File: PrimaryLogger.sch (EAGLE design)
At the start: 48 parts, among them J1 CONN_42.54_SCREW, J2 CONN_42.54_SCREW, J3 CONN_42.54_SCREW, J4 CONN_42.54_SCREW, J5 CONN_32.54_SCREW, U1 MIC2005, U2 MIC2091, U25 SN74AUP3G34DCU, U3 TPL5010DDC, U4 TXS0102DCU, U5 SN74LVC1G3157DRL, U6 TCS3400, U7 SHTC3DFN

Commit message: Continued layout progress
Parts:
- C1, C2: value (none) -> 6pF
- XTAL1: DIGIKEY (none) -> 535-11937-1-ND; MF (none) -> ABS07-120-32.768KHZ-T; MPN (none) -> Abracon
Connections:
- new net GPIOXA: J5.2, MS1.GPIOA3
- new net N$10: MS1.GPIOA5
- new net N$9: MS1.GPIOA4
- net 3V3_EXT: now also J5.1
- net GND: now also J5.3
- net GPIO1A: now also MS1.GPIOA0
- net GPIO2A: now also MS1.GPIOA1
- net GPIO3A: now also MS1.GPIOA2
- net MISO: now also MS1.GPIOMISO
- net MOSI: now also MS1.GPIOMOSI
- net SCK: now also MS1.GPIOSCK
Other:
- moved on the sheet: J6, J7, J8, R8

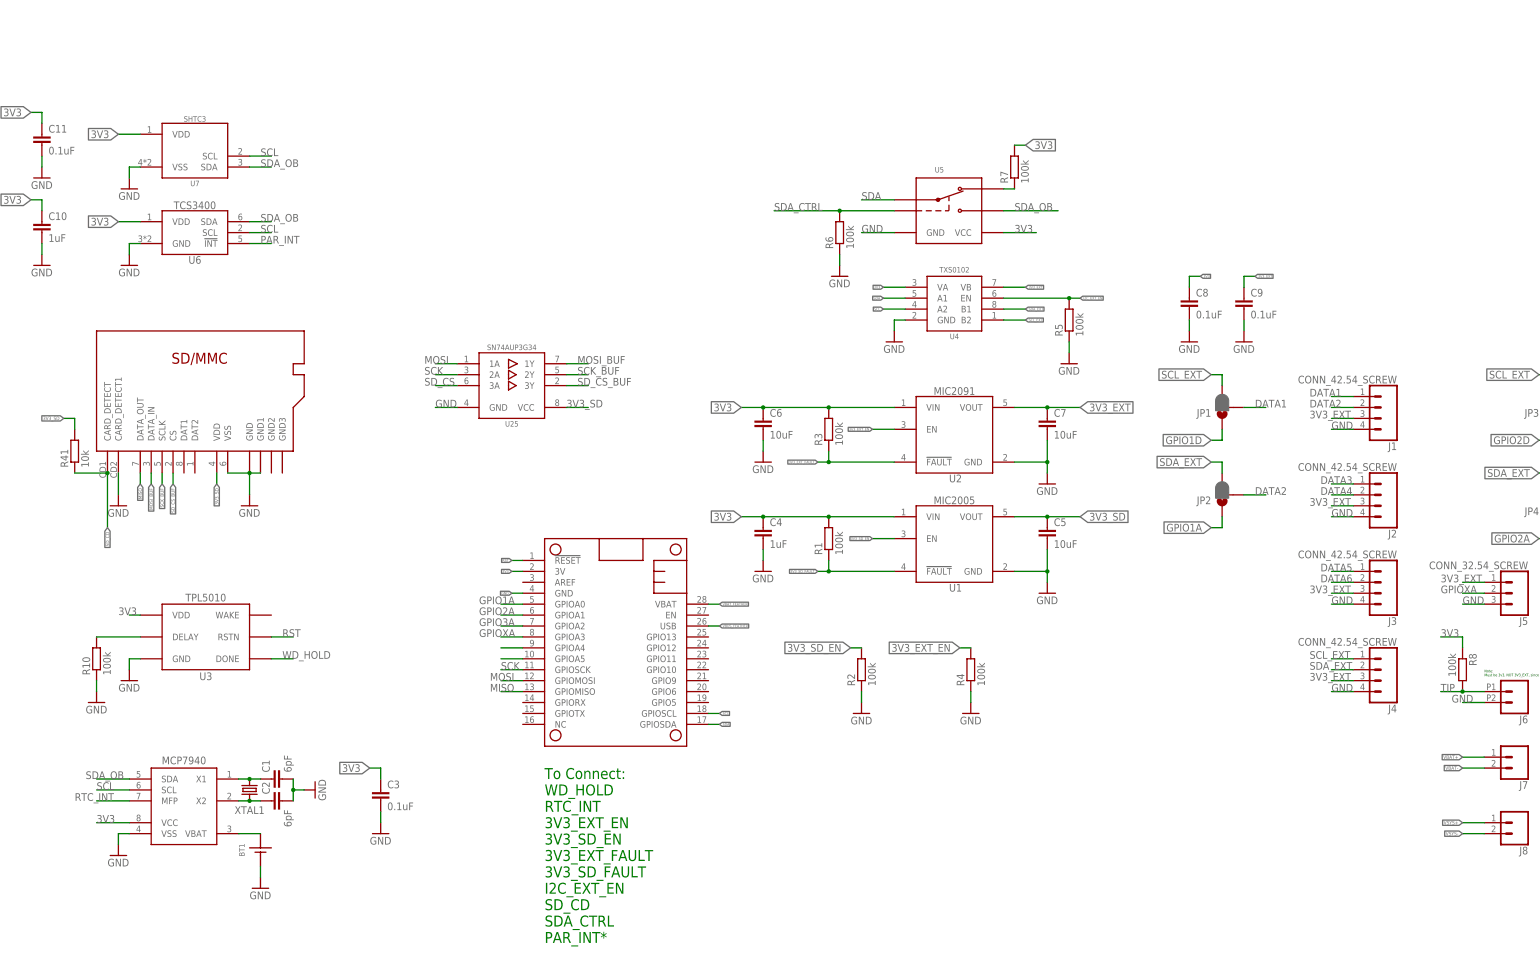
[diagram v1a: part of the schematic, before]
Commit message: Continued layout and preliminary board capture
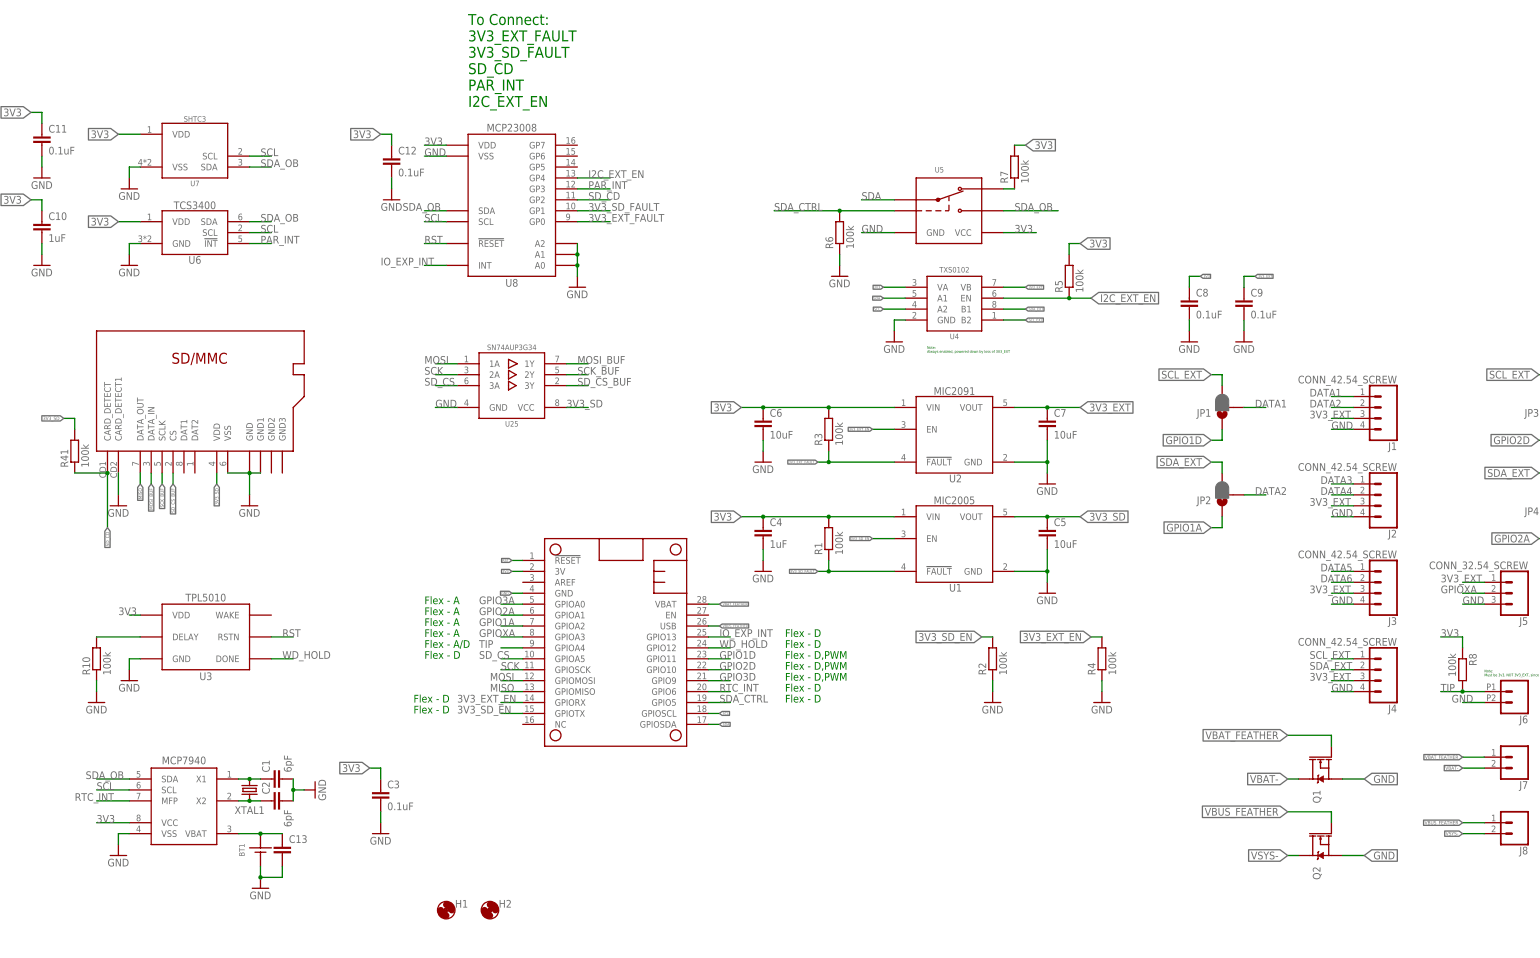
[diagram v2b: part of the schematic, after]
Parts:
- added C12: 0.1uF, bschulz_passives:C-EU0.1UFC0603
- added C13: (no value), bschulz_passives:C-EU0.1UFC0603
- added H1, H2: (no value), bschulz:MOUNTING_HOLE4_NP
- added Q1, Q2: DMG3404, bschulz:MOSFET-NCH-DMG3404L
- added U8: MCP23008QFN, bschulz:MCP23008QFN
- C1, C2: device bschulz_passives:C-EUC0603 -> bschulz_passives:C-EUC0402
- R10: device bschulz_passives:R-EU_100KR0402 -> bschulz_passives:R-EU_100KR0603
- R41: value 10k -> 100k; device bschulz_passives:R-EU_10KR0402 -> bschulz_passives:R-EU_100KR0603
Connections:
- removed net N$10: MS1.GPIOA5
- removed net N$9: MS1.GPIOA4
- removed net VBAT+: J7.1
- removed net VSYS+: J8.1
- new net IO_EXP_INT: MS1.GPIO13, U8.INT
- net 3V3: now also C12.1, R5.2, U8.VDD
- net 3V3_EXT_EN: now also MS1.GPIORX
- net 3V3_EXT_FAULT: now also U8.GP0
- net 3V3_SD_EN: now also MS1.GPIOTX
- net 3V3_SD_FAULT: now also U8.GP1
- net GND: now also C12.2, C13.2, Q1.S, Q2.S, U8.A0, U8.A1, U8.A2, U8.VSS; no longer R5.1
- net GPIO1A: now also MS1.GPIOA2; no longer MS1.GPIOA0
- net GPIO1D: now also MS1.GPIO11
- net GPIO2D: now also MS1.GPIO10
- net GPIO3A: now also MS1.GPIOA0; no longer MS1.GPIOA2
- net GPIO3D: now also MS1.GPIO9
- net I2C_EXT_EN: now also R5.1, U8.GP4; no longer R5.2
- net PAR_INT: now also U8.GP3
- net RST: now also U8.!RESET
- net RTC_INT: now also MS1.GPIO6
- net SCL: now also U8.SCL
- net SDA_CTRL: now also MS1.GPIO5
- net SDA_OB: now also U8.SDA
- net SD_CD: now also U8.GP2
- net SD_CS: now also MS1.GPIOA5
- net TIP: now also MS1.GPIOA4
- net VBAT: now also C13.1
- net VBAT-: now also Q1.D
- net VBAT_FEATHER: now also J7.1, Q1.G
- net VBUS_FEATHER: now also J8.1, Q2.G
- net VSYS-: now also Q2.D
- net WD_HOLD: now also MS1.GPIO12
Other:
- note added: "Flex - A"
- note added: "Flex - A/D"
- note added: "Flex - D"
- note added: "Flex - D,PWM"
- note added: "Note: Always enabled, powered down by loss of 3V3_EXT"
- note added: "To Connect: 3V3_EXT_FAULT 3V3_SD_FAULT SD_CD PAR_INT I2C_EXT_EN"
- note removed: "To Connect: WD_HOLD RTC_INT 3V3_EXT_EN 3V3_SD_EN 3V3_EXT_FAULT 3V3_SD_FAULT I2C_EXT_EN SD_CD SDA_CTRL PAR_INT*"
- moved on the sheet: R2, R4, R5

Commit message: BETA preliminary layout
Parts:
- renumbered U$1 to U9
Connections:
- net 3V3_EXT_EN: now also MS1.GPIO13; no longer MS1.GPIORX
- net GND: now also SD1.GND2, SD1.GND3
- net I2C_EXT_EN: now also U8.GP3; no longer U8.GP4
- net IO_EXP_INT: now also MS1.GPIORX; no longer MS1.GPIO13
- net PAR_INT: now also U8.GP4; no longer U8.GP3
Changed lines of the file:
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@@
 </classes>
 <parts>
-<part name="U$1" library="bschulz" deviceset="MCP7940" device="SOIC"/>
+<part name="U9" library="bschulz" deviceset="MCP7940" device="SOIC"/>
 <part name="XTAL1" library="bschulz" deviceset="CRYSTAL" device="3.2X1.5">
 <attribute name="DIGIKEY" value="535-11937-1-ND"/>
@@
 </plain>
 <instances>
-<instance part="U$1" gate="G$1" x="30.48" y="40.64" smashed="yes"/>
+<instance part="U9" gate="G$1" x="30.48" y="40.64" smashed="yes"/>
 <instance part="XTAL1" gate="G$1" x="48.26" y="43.18" smashed="yes" rot="R270">
 <attribute name="NAME" x="48.26" y="37.592" size="1.778" layer="95" font="vector" align="bottom-center"/>
@@
 <net name="N$1" class="0">
 <segment>
-<pinref part="U$1" gate="G$1" pin="X1"/>
+<pinref part="U9" gate="G$1" pin="X1"/>
 <pinref part="XTAL1" gate="G$1" pin="1"/>
 <wire x1="45.72" y1="45.72" x2="48.26" y2="45.72" width="0.1524" layer="91"/>
@@
 <net name="N$2" class="0">
 <segment>
-<pinref part="U$1" gate="G$1" pin="X2"/>
+<pinref part="U9" gate="G$1" pin="X2"/>
 <pinref part="XTAL1" gate="G$1" pin="2"/>
 <wire x1="45.72" y1="40.64" x2="48.26" y2="40.64" width="0.1524" layer="91"/>
@@
 </segment>
 <segment>
-<pinref part="U$1" gate="G$1" pin="VSS"/>
+<pinref part="U9" gate="G$1" pin="VSS"/>
 <wire x1="20.32" y1="33.02" x2="17.78" y2="33.02" width="0.1524" layer="91"/>
 <wire x1="17.78" y1="33.02" x2="17.78" y2="30.48" width="0.1524" layer="91"/>
@@
 <pinref part="GND44" gate="1" pin="GND"/>
 <wire x1="48.26" y1="111.76" x2="48.26" y2="116.84" width="0.1524" layer="91"/>
+<pinref part="SD1" gate="G$1" pin="GND2"/>
+<wire x1="50.8" y1="116.84" x2="53.34" y2="116.84" width="0.1524" layer="91"/>
+<junction x="50.8" y="116.84"/>
+<pinref part="SD1" gate="G$1" pin="GND3"/>
+<wire x1="53.34" y1="116.84" x2="55.88" y2="116.84" width="0.1524" layer="91"/>
+<junction x="53.34" y="116.84"/>
 </segment>
 <segment>
@@
 <net name="SCL" class="0">
 <segment>
-<pinref part="U$1" gate="G$1" pin="SCL"/>
+<pinref part="U9" gate="G$1" pin="SCL"/>
 <wire x1="20.32" y1="43.18" x2="12.7" y2="43.18" width="0.1524" layer="91"/>
 <label x="12.7" y="43.18" size="1.778" layer="95"/>
@@
 <net name="RTC_INT" class="0">
 <segment>
-<pinref part="U$1" gate="G$1" pin="MFP"/>
+<pinref part="U9" gate="G$1" pin="MFP"/>
 <wire x1="20.32" y1="40.64" x2="12.7" y2="40.64" width="0.1524" layer="91"/>
 <label x="7.62" y="40.64" size="1.778" layer="95"/>
@@
 <segment>
 <pinref part="BT1" gate="G$1" pin="+"/>
-<pinref part="U$1" gate="G$1" pin="VBAT"/>
+<pinref part="U9" gate="G$1" pin="VBAT"/>
 <wire x1="50.8" y1="33.02" x2="45.72" y2="33.02" width="0.1524" layer="91"/>
 <pinref part="C13" gate="G$1" pin="1"/>
@@
 </segment>
 <segment>
-<pinref part="U$1" gate="G$1" pin="VCC"/>
+<pinref part="U9" gate="G$1" pin="VCC"/>
 <wire x1="20.32" y1="35.56" x2="12.7" y2="35.56" width="0.1524" layer="91"/>
 <label x="12.7" y="35.56" size="1.778" layer="95"/>
@@
 </segment>
 <segment>
-<pinref part="MS1" gate="G$1" pin="GPIORX"/>
-<wire x1="111.76" y1="63.5" x2="106.68" y2="63.5" width="0.1524" layer="91"/>
-<label x="96.52" y="63.5" size="1.778" layer="95"/>
+<pinref part="MS1" gate="G$1" pin="GPIO13"/>
+<wire x1="154.94" y1="78.74" x2="160.02" y2="78.74" width="0.1524" layer="91"/>
+<label x="157.48" y="78.74" size="1.778" layer="95"/>
 </segment>
 </net>
@@
 <net name="SDA_OB" class="0">
 <segment>
-<pinref part="U$1" gate="G$1" pin="SDA"/>
+<pinref part="U9" gate="G$1" pin="SDA"/>
 <wire x1="20.32" y1="45.72" x2="12.7" y2="45.72" width="0.1524" layer="91"/>
 <label x="10.16" y="45.72" size="1.778" layer="95"/>
@@
 </segment>
 <segment>
-<pinref part="U8" gate="G$1" pin="GP3"/>
-<wire x1="124.46" y1="182.88" x2="132.08" y2="182.88" width="0.1524" layer="91"/>
-<label x="127" y="182.88" size="1.778" layer="95"/>
+<pinref part="U8" gate="G$1" pin="GP4"/>
+<wire x1="124.46" y1="185.42" x2="132.08" y2="185.42" width="0.1524" layer="91"/>
+<label x="127" y="185.42" size="1.778" layer="95"/>
 </segment>
 </net>
@@
 </segment>
 <segment>
-<pinref part="U8" gate="G$1" pin="GP4"/>
-<wire x1="124.46" y1="185.42" x2="132.08" y2="185.42" width="0.1524" layer="91"/>
-<label x="127" y="185.42" size="1.778" layer="95"/>
+<pinref part="U8" gate="G$1" pin="GP3"/>
+<wire x1="124.46" y1="182.88" x2="132.08" y2="182.88" width="0.1524" layer="91"/>
+<label x="127" y="182.88" size="1.778" layer="95"/>
 </segment>
 </net>
@@
 </segment>
 <segment>
-<pinref part="MS1" gate="G$1" pin="GPIO13"/>
-<wire x1="154.94" y1="78.74" x2="160.02" y2="78.74" width="0.1524" layer="91"/>
-<label x="157.48" y="78.74" size="1.778" layer="95"/>
-</segment>
-</net>
+<pinref part="MS1" gate="G$1" pin="GPIORX"/>
+<wire x1="111.76" y1="63.5" x2="106.68" y2="63.5" width="0.1524" layer="91"/>
+<label x="96.52" y="63.5" size="1.778" layer="95"/>
+</segment>
+</net>
